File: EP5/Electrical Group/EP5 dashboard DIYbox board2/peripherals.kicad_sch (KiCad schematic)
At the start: 54 parts, among them IC2 LSF0204DPWR, IC3 TCAN1057AVDRQ1, J2 screen, J3 ext_connector, J4 CAN, Q1 BSS84AK

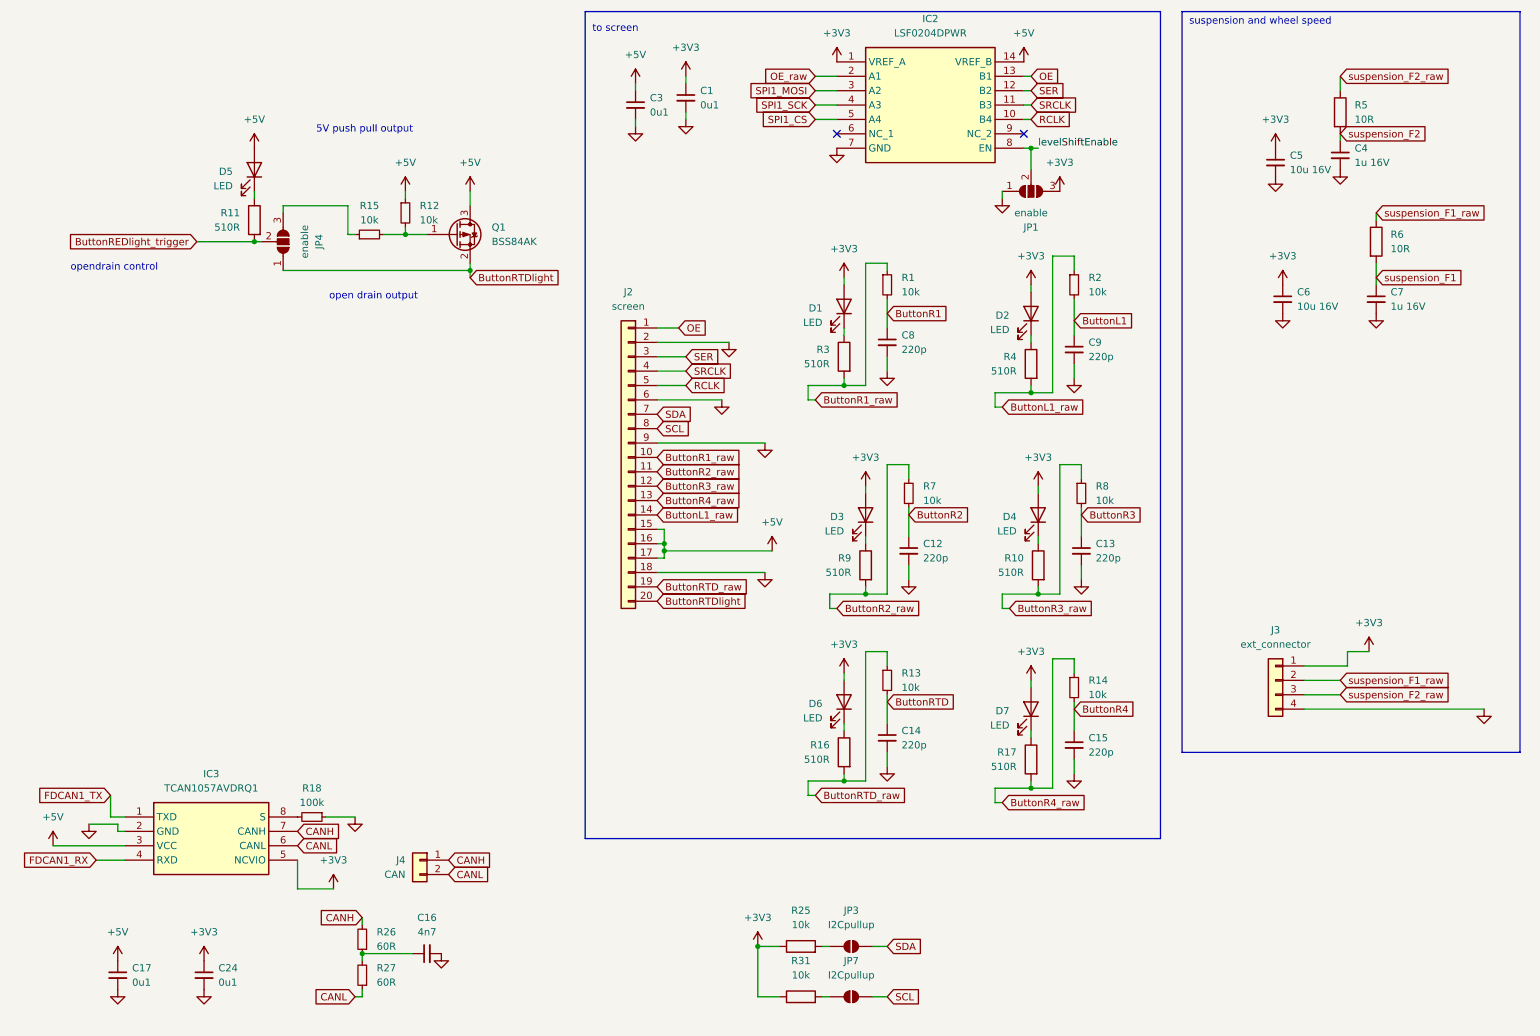
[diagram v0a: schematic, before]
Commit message: update dashboard 2 to V4.0 in EP5
this is a version using stm32H562
previously only use nucleo G431
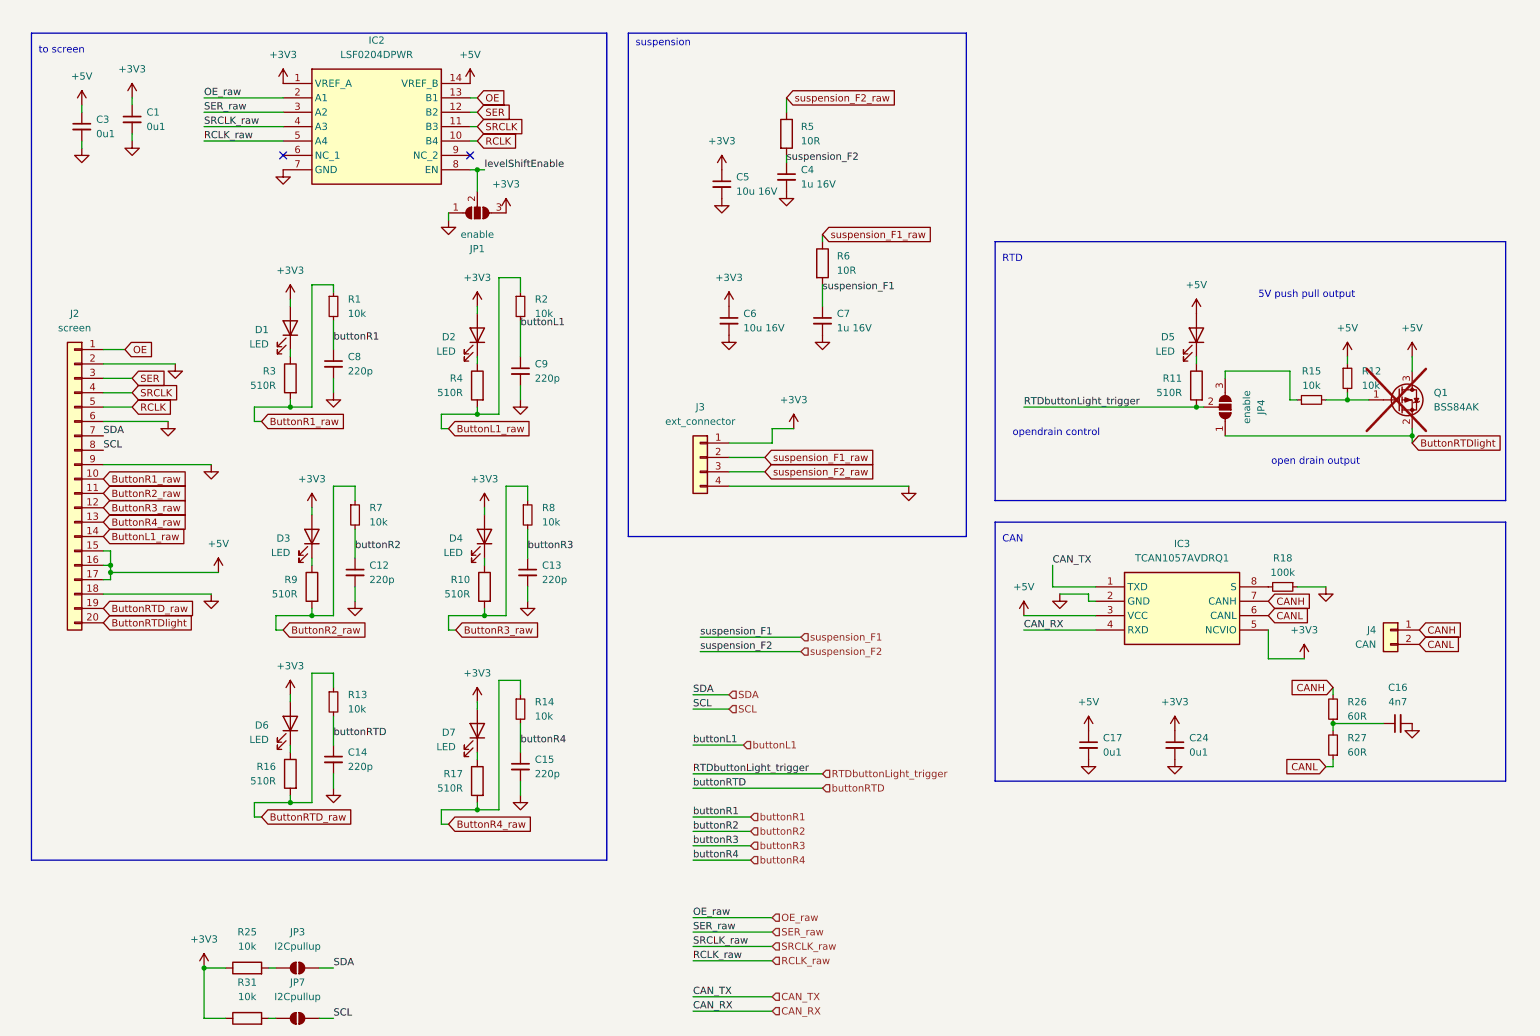
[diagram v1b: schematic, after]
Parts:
- Q1: now not fitted
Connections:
- net ButtonL1 renamed buttonL1
- net ButtonR1 renamed buttonR1
- net ButtonR2 renamed buttonR2
- net ButtonR3 renamed buttonR3
- net ButtonR4 renamed buttonR4
- net ButtonREDlight_trigger renamed RTDbuttonLight_trigger
- net ButtonRTD renamed buttonRTD
- net FDCAN1_RX renamed CAN_RX
- net FDCAN1_TX renamed CAN_TX
- net SPI1_CS renamed RCLK_raw
- net SPI1_MOSI renamed SER_raw
- net SPI1_SCK renamed SRCLK_raw
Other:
- note added: "CAN"
- note added: "RTD"
- note added: "suspension"
- note removed: "suspension and wheel speed"
- moved on the sheet: C1, C12, C13, C14, C15, C16, C17, C24, C3, C4, C5, C6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
